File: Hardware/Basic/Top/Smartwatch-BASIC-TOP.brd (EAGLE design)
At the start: 38 x 38 mm, 60 parts, among them SW6 SWITCH.MOM, SW7 SWITCH.MOM, U2 NRF52832_MODULE_MDBT42, U4 FT231XS

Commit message: Top Board Routed
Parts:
- removed C20, C21: 4.7u, LinnesLab-Passives:C0603
- removed C5, C6: 1u, LinnesLab-Passives:C0603
- removed CHRG2: MCP73831, LinnesLab-Power:SOT23-5
- removed LDO2: MIC5504, LinnesLab-Power:SOT23-5
- removed R11: (no value), LinnesLab-Passives:R0603
- removed R12, R15: 100k, LinnesLab-Passives:R0603
- removed SD2: (no value), LinnesLab-Connectors:MICROSD
- moved C14 23.5 mm to (32.9, 13.3)
- moved D1 19.8 mm to (34.6, 12.7), turned to 270 degrees
- moved SW3 19.1 mm to (34.9, 34.8), turned to 90 degrees
- moved R5 16.1 mm to (36.3, 12.9), turned to 270 degrees
- moved LED3 15.3 mm to (34.2, 20.9), turned to 270 degrees
- moved LED4 15.0 mm to (35.8, 20.9), turned to 270 degrees
- moved C17 12.4 mm to (3.27, 19.0)
- moved C19 12.4 mm to (1.95, 19.1)
- moved SW4 12.3 mm to (35.0, 17.0), turned to 270 degrees
- moved CORTEX1 12.0 mm to (35.3, 28.9), turned to 270 degrees
- moved R3 11.3 mm to (33.6, 24.0), turned to 90 degrees
- moved R4 9.96 mm to (36.3, 24.0), turned to 90 degrees
- moved SW7 9.21 mm to (21.9, 4.24), turned to 180 degrees
- moved C11 9.17 mm to (35.4, 9.68), turned to 180 degrees
- moved SW6 8.45 mm to (31.9, 4.24), turned to 180 degrees
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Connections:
- removed net CD2: SD2.CD2
- removed net N$17: CHRG2.5, R11.2
- net 3.3V: no longer C6.1, LDO2.5, R15.2, SD2.4
- net D27/CHRG.STAT: no longer CHRG2.1, R12.1
- net D5/CD1: no longer SD2.CD1
- net D7/SD.CS: no longer SD2.2
- net GND: no longer C20.2, C21.1, C5.1, C6.2, CHRG2.2, LDO2.2, R11.1, R15.1, SD2.6, SD2.MT1, SD2.MT2
- net MISO: no longer SD2.7
- net MOSI: no longer SD2.3
- net SCK: no longer SD2.5
- net VIN: no longer C21.2, C5.2, CHRG2.4, LDO2.1, LDO2.3, R12.2
- net VLIPO: no longer C20.1, CHRG2.3
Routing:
- net SCK: track 59.4 -> 17.7 mm, vias 2 -> 0
- net D27/CHRG.STAT: track 33.4 -> 0.00 mm, vias 1 -> 0
- net D7/SD.CS: track 31.7 -> 3.52 mm
- net MOSI: track 42.1 -> 15.0 mm, vias 5 -> 2
- net RESET: track 0.00 -> 26.1 mm, vias 0 -> 2
- net GND: track 90.5 -> 113.5 mm, vias 22 -> 23
- net D3/RESET.OLED: track 34.8 -> 12.8 mm
- net 3.3V: track 58.4 -> 38.2 mm, vias 13 -> 11
- net MISO: track 19.6 -> 0.00 mm, vias 3 -> 0
- net P0.09/NFC1: track 3.11 -> 19.9 mm, vias 0 -> 2
- net VIN: track 31.4 -> 15.3 mm
- net D5/CD1: track 14.4 -> 0.00 mm, vias 1 -> 0
- net LED2: track 0.00 -> 13.0 mm, vias 0 -> 2
- net RXD: track 29.0 -> 40.4 mm
- net N$2: track 3.22 -> 14.0 mm, vias 0 -> 2
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
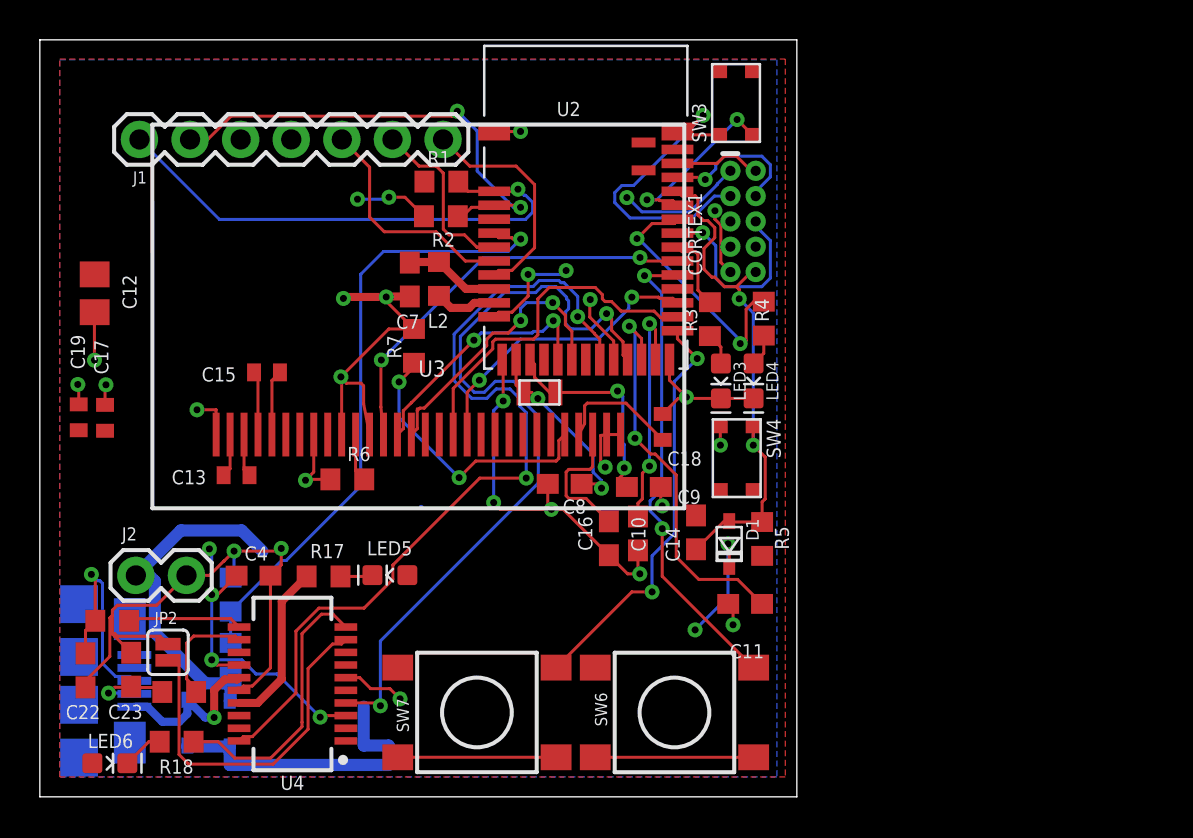
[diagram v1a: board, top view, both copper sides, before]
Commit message: Rearranging Top Board
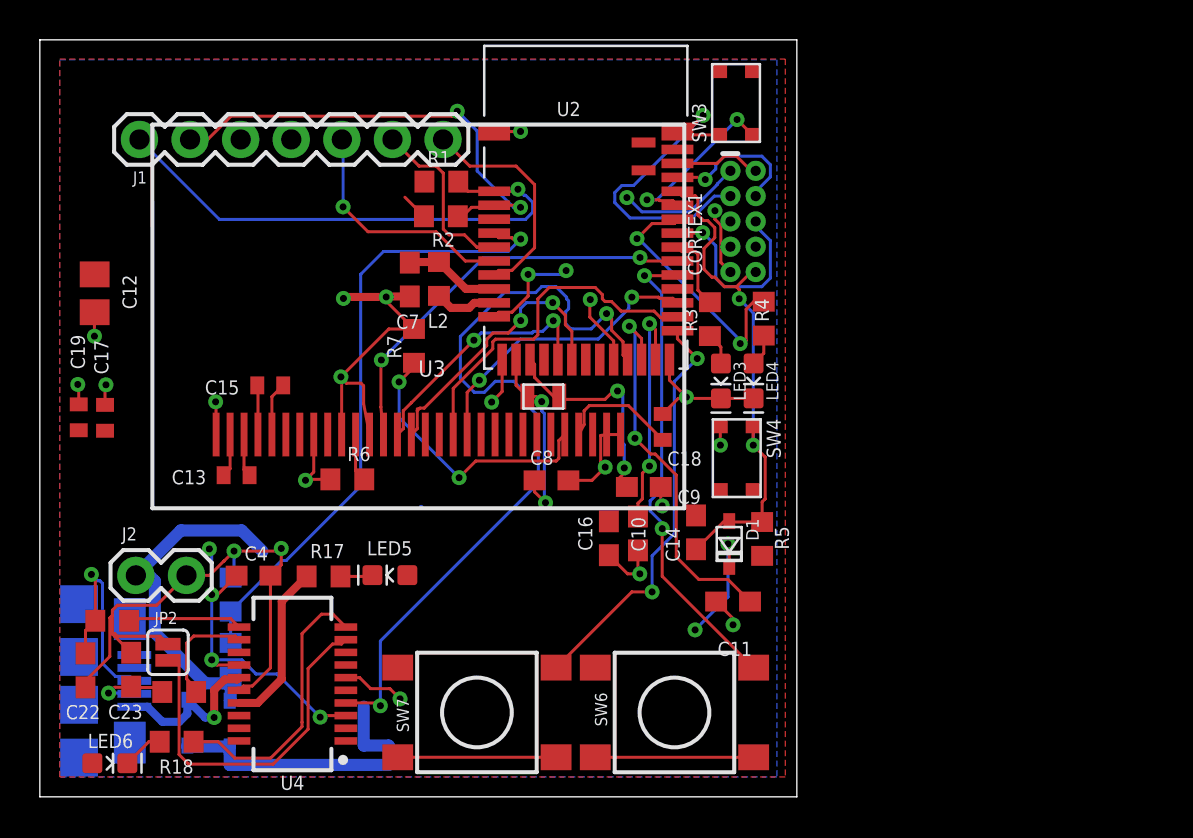
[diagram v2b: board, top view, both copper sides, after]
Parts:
- moved C8 0.69 mm to (25.7, 15.9), turned to 180 degrees
- moved C15 0.67 mm to (11.6, 20.7)
- moved C11 0.62 mm to (34.8, 9.80)
- moved XTAL2 0.28 mm to (25.3, 20.1)
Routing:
- net TXD: track 43.9 -> 0.00 mm, vias 2 -> 0
- net GND: track 113.5 -> 101.0 mm, vias 23 -> 21
- net N$13: track 7.57 -> 0.00 mm
- net 3.3V: track 38.2 -> 35.8 mm, vias 11 -> 9
- net N$7: track 3.20 -> 2.48 mm
- net P0.09/NFC1: track 19.9 -> 19.2 mm
- net N$8: track 3.29 -> 2.70 mm
- net A6/TIA: track 11.6 -> 12.1 mm, vias 0 -> 1

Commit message: Rearranged Top Board
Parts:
- moved C9 3.18 mm to (28.1, 13.3), turned to 270 degrees
- moved C16 3.01 mm to (30.3, 15.4), turned to 180 degrees
- moved C18 0.91 mm to (31.2, 19.5)
- moved C11 0.43 mm to (35.2, 9.89), turned to 0 degrees
- moved R7 0.19 mm to (18.9, 22.8)
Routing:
- net TXD: track 0.00 -> 32.8 mm, vias 0 -> 2
- net 3.3V: track 35.8 -> 29.6 mm, vias 9 -> 7
- net LED2: track 13.0 -> 9.38 mm
- net N$13: track 0.00 -> 3.44 mm
- net GND: track 101.0 -> 98.6 mm
- net VIN: track 15.3 -> 13.3 mm
- net N$6: track 11.1 -> 10.0 mm
- net USB-: track 4.77 -> 4.04 mm
- net SDA: track 26.3 -> 26.9 mm

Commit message: Rearranged Top Board
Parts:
- added C1, C3: 4.7u, LinnesLab-Passives:C0603
- added C5, C6: 1u, LinnesLab-Passives:C0603
- added CHRG2: MCP73831, LinnesLab-Power:SOT23-5
- added LDO2: MIC5504, LinnesLab-Power:SOT23-5
- added R11: (no value), LinnesLab-Passives:R0603
- added R12, R8: 100k, LinnesLab-Passives:R0603
- moved C12 6.90 mm to (2.32, 32.2)
- moved C17 5.82 mm to (3.08, 13.2)
- moved C19 5.82 mm to (1.76, 13.2)
- moved C18 0.71 mm to (31.6, 20.1), turned to 180 degrees
- moved XTAL2 0.20 mm to (25.1, 20.2)
- moved R2 0.14 mm to (20.1, 29.0)
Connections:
- new net N$16: CHRG2.5, R11.2
- new net VIN1: C1.2, C5.2, CHRG2.4, LDO2.1, LDO2.3, R12.2
- net 3.3V: now also C6.1, LDO2.5, R8.2
- net D27/CHRG.STAT: now also CHRG2.1, R12.1
- net GND: now also C1.1, C3.2, C5.1, C6.2, CHRG2.2, LDO2.2, R11.1, R8.1
- net VLIPO: now also C3.1, CHRG2.3
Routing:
- net D27/CHRG.STAT: track 0.00 -> 26.5 mm, vias 0 -> 2
- net 3.3V: track 29.6 -> 9.59 mm, vias 7 -> 1
- net RXD: track 40.4 -> 24.9 mm
- net VIN1: track 0.00 -> 13.5 mm
- net VLIPO: track 17.6 -> 11.3 mm
- net USB+: track 11.0 -> 4.91 mm
- net SCL: track 23.6 -> 17.5 mm, vias 2 -> 0
- net SDA: track 26.9 -> 21.5 mm, vias 1 -> 0
- net A4/BATT: track 31.6 -> 26.5 mm
- net GND: track 98.6 -> 94.3 mm, vias 21 -> 29
- net P0.09/NFC1: track 19.5 -> 15.2 mm
- net A6/TIA: track 12.1 -> 15.9 mm, vias 1 -> 0
- net P0.10/NFC2: track 11.8 -> 8.74 mm, vias 2 -> 0
- net TXD: track 32.8 -> 35.3 mm
- net A7/PPG: track 11.6 -> 9.55 mm, vias 0 -> 1
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
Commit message: Fixing top board issues
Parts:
- moved C19 6.21 mm to (7.96, 12.9), turned to 90 degrees
- moved J2 5.11 mm to (2.34, 12.1), turned to 90 degrees
- moved C17 3.58 mm to (6.64, 12.9), turned to 90 degrees
- moved LED4 0.30 mm to (35.5, 20.9)
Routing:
- net VIN: track 12.1 -> 2.17 mm
- net VLIPO: track 11.3 -> 18.0 mm
- net 3.3V: track 9.59 -> 6.37 mm
- net GND: track 94.3 -> 96.6 mm, vias 29 -> 30
- net D4/DC.OLED: track 14.2 -> 15.2 mm
- net N$4: track 9.45 -> 8.87 mm
- net A6/TIA: track 15.9 -> 16.5 mm
- net D3/RESET.OLED: track 12.8 -> 13.3 mm
- net D11/SW1: track 22.0 -> 22.5 mm

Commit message: Top Board Complete
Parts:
- moved C19 11.8 mm to (2.93, 2.28)
- moved C17 11.8 mm to (1.61, 2.30)
- moved C23 5.45 mm to (6.56, 11.5), turned to 180 degrees
- moved R10 3.81 mm to (8.19, 8.88), turned to 270 degrees
- moved LED6 2.80 mm to (4.55, 4.29), turned to 270 degrees
- moved C22 2.10 mm to (3.91, 7.69), turned to 0 degrees
- moved C1 1.48 mm to (6.17, 17.5)
- moved R18 0.98 mm to (6.97, 3.74)
- moved C11 0.59 mm to (35.4, 9.33)
- moved R16 0.43 mm to (3.98, 9.09)
- moved C9 0.42 mm to (27.6, 13.4)
- moved XTAL2 0.07 mm to (25.0, 20.2)
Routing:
- net USB-: track 4.37 -> 13.6 mm
- net GND: track 96.6 -> 88.5 mm, vias 30 -> 29
- net USB+: track 4.91 -> 8.57 mm
- net N$25: track 4.23 -> 1.87 mm
- net V_USB: track 8.63 -> 7.15 mm
- net !CTS: track 18.5 -> 17.6 mm
- net N$4: track 8.87 -> 8.02 mm
- net RESET: track 26.1 -> 25.3 mm
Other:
- board text added: "+"

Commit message: Organized Schematics and Silkscreens for both boards
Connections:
- removed net VIN1: C1.2, C5.2, CHRG2.4, LDO2.1, LDO2.3, R12.2
- net VIN: now also C1.2, C5.2, CHRG2.4, LDO2.1, LDO2.3, R12.2
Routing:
- net VIN: track 2.17 -> 15.6 mm
- net VIN1: track 13.4 -> 0.00 mm
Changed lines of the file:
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@@
 <wire x1="3.175" y1="25.679396875" x2="3.210559375" y2="25.71495625" width="0.1524" layer="1"/>
 <via x="3.210559375" y="25.71495625" extent="1-16" drill="0.35"/>
-<wire x1="32.231678125" y1="20.0924" x2="32.355875" y2="20.216596875" width="0.1524" layer="1"/>
 <wire x1="3.6846375" y1="16.863059375" x2="3.971659375" y2="16.5760375" width="0.1524" layer="1"/>
 <wire x1="3.971659375" y1="16.5760375" x2="4.91744375" y2="16.576040625" width="0.1524" layer="1"/>
@@
 <wire x1="7.404865625" y1="2.57514375" x2="7.404865625" y2="2.52688125" width="0.6096" layer="16"/>
 <wire x1="7.404865625" y1="2.52688125" x2="9.530840625" y2="2.52688125" width="0.6096" layer="16"/>
+<contactref element="C5" pad="2"/>
+<contactref element="LDO2" pad="1"/>
+<contactref element="LDO2" pad="3"/>
+<contactref element="CHRG2" pad="4"/>
+<contactref element="C1" pad="2"/>
+<contactref element="R12" pad="2"/>
+<wire x1="4.563996875" y1="18.5953" x2="5.90718125" y2="18.5953" width="0.6096" layer="1"/>
+<wire x1="6.1696625" y1="18.33281875" x2="5.90718125" y2="18.5953" width="0.6096" layer="1"/>
+<wire x1="4.563996875" y1="18.5953" x2="3.48651875" y2="19.672778125" width="0.6096" layer="1"/>
+<wire x1="3.48651875" y1="19.672778125" x2="3.48651875" y2="22.0370375" width="0.6096" layer="1"/>
+<wire x1="4.125" y1="24.56979375" x2="4.125" y2="22.67551875" width="0.6096" layer="1"/>
+<wire x1="4.125" y1="22.67551875" x2="3.48651875" y2="22.0370375" width="0.6096" layer="1"/>
+<wire x1="5.95375625" y1="24.2350375" x2="5.619" y2="24.56979375" width="0.6096" layer="1"/>
+<wire x1="5.619" y1="24.56979375" x2="4.125" y2="24.56979375" width="0.6096" layer="1"/>
+<wire x1="2.225" y1="24.56979375" x2="2.4428" y2="24.35199375" width="0.6096" layer="1"/>
+<wire x1="2.4428" y1="24.35199375" x2="2.4428" y2="23.7804125" width="0.6096" layer="1"/>
+<wire x1="3.48651875" y1="22.73669375" x2="3.48651875" y2="22.0370375" width="0.6096" layer="1"/>
+<wire x1="2.4428" y1="23.7804125" x2="3.48651875" y2="22.73669375" width="0.6096" layer="1"/>
+<wire x1="7.404865625" y1="2.57514375" x2="6.1696625" y2="18.33281875" width="0" layer="19" extent="1-16"/>
 </signal>
 <signal name="N$21">
@@
 <wire x1="4.563996875" y1="21.36011875" x2="5.17741875" y2="21.973540625" width="0.1524" layer="1"/>
 </signal>
-<signal name="VIN1">
-<contactref element="C5" pad="2"/>
-<contactref element="LDO2" pad="1"/>
-<contactref element="LDO2" pad="3"/>
-<contactref element="CHRG2" pad="4"/>
-<contactref element="C1" pad="2"/>
-<contactref element="R12" pad="2"/>
-<wire x1="4.563996875" y1="18.5953" x2="5.90718125" y2="18.5953" width="0.6096" layer="1"/>
-<wire x1="6.1696625" y1="18.33281875" x2="5.90718125" y2="18.5953" width="0.6096" layer="1"/>
-<wire x1="4.563996875" y1="18.5953" x2="3.48651875" y2="19.672778125" width="0.6096" layer="1"/>
-<wire x1="3.48651875" y1="19.672778125" x2="3.48651875" y2="22.0370375" width="0.6096" layer="1"/>
-<wire x1="4.125" y1="24.56979375" x2="4.125" y2="22.67551875" width="0.6096" layer="1"/>
-<wire x1="4.125" y1="22.67551875" x2="3.48651875" y2="22.0370375" width="0.6096" layer="1"/>
-<wire x1="5.95375625" y1="24.2350375" x2="5.619" y2="24.56979375" width="0.6096" layer="1"/>
-<wire x1="5.619" y1="24.56979375" x2="4.125" y2="24.56979375" width="0.6096" layer="1"/>
-<wire x1="2.225" y1="24.56979375" x2="2.4428" y2="24.35199375" width="0.6096" layer="1"/>
-<wire x1="2.4428" y1="24.35199375" x2="2.4428" y2="23.7804125" width="0.6096" layer="1"/>
-<wire x1="3.48651875" y1="22.73669375" x2="3.48651875" y2="22.0370375" width="0.6096" layer="1"/>
-<wire x1="2.4428" y1="23.7804125" x2="3.48651875" y2="22.73669375" width="0.6096" layer="1"/>
-</signal>
 </signals>

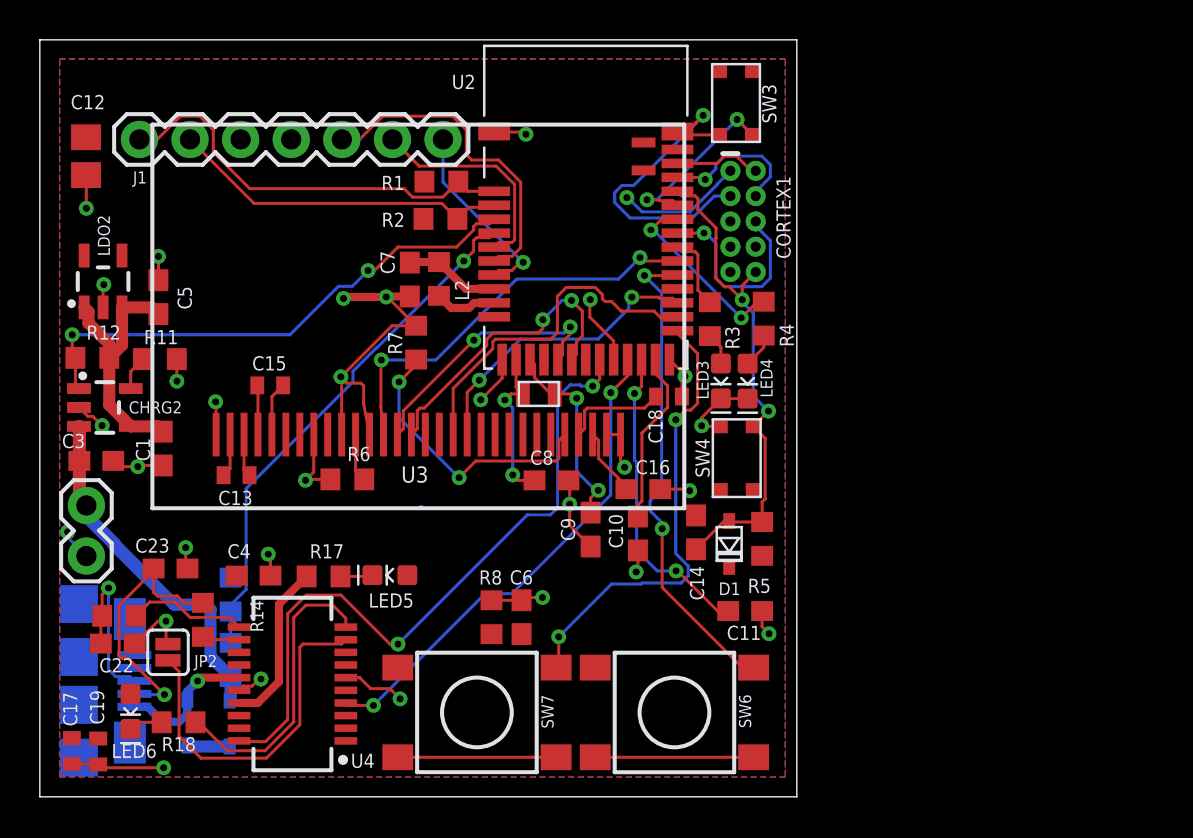
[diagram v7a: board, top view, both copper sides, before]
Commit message: Fixed Top Board Issue
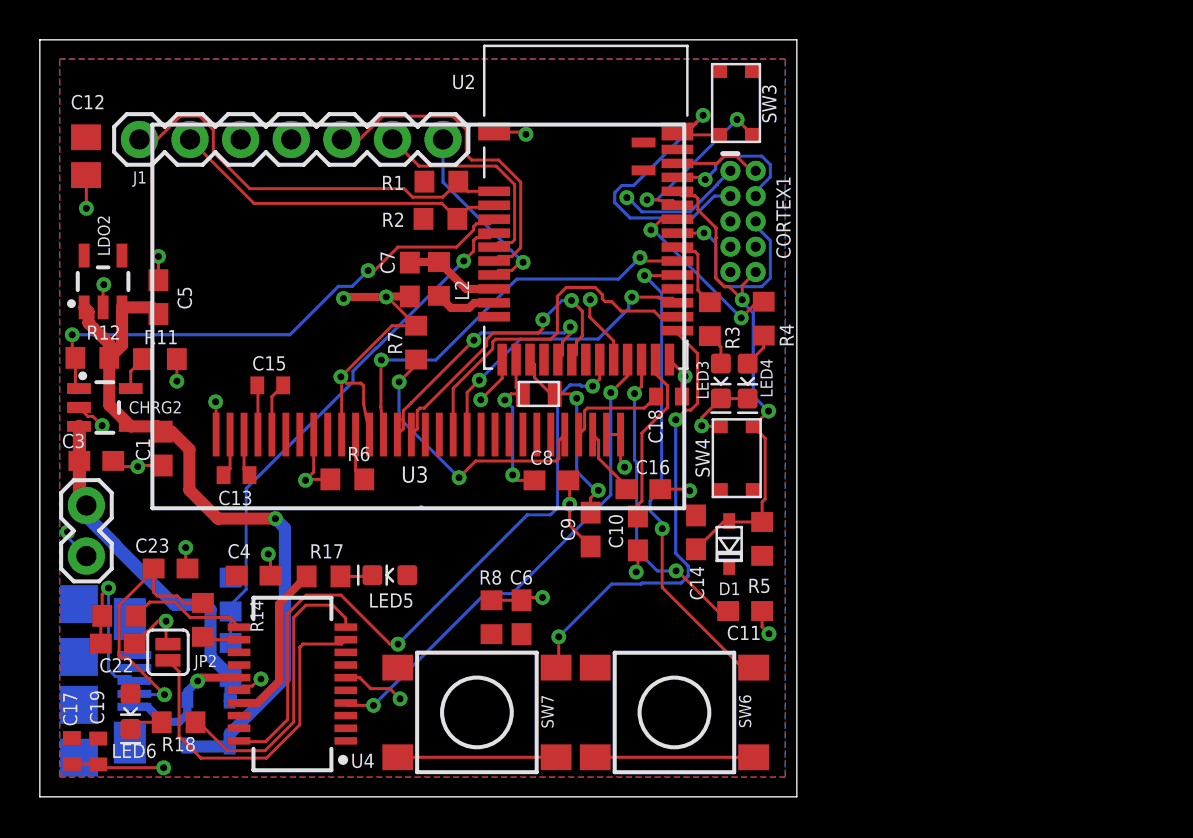
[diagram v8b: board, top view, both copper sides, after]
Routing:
- net VIN: track 15.6 -> 37.0 mm, vias 0 -> 1
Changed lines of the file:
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@@
 <drawing>
 <settings>
-<setting alwaysvectorfont="no"/>
+<setting alwaysvectorfont="yes"/>
 <setting verticaltext="up"/>
 </settings>
@@
 <via x="18.082259375" y="4.91998125" extent="1-16" drill="0.35"/>
 <contactref element="J1" pad="3"/>
-<wire x1="32.006" y1="33.397" x2="32.0942" y2="33.4852" width="0.1524" layer="1"/>
 <wire x1="18.570740625" y1="25.1173625" x2="17.4117625" y2="25.1173625" width="0.4064" layer="1"/>
 <wire x1="17.4117625" y1="25.1173625" x2="17.387059375" y2="25.092659375" width="0.4064" layer="1"/>
@@
 <wire x1="3.48651875" y1="22.73669375" x2="3.48651875" y2="22.0370375" width="0.6096" layer="1"/>
 <wire x1="2.4428" y1="23.7804125" x2="3.48651875" y2="22.73669375" width="0.6096" layer="1"/>
-<wire x1="7.404865625" y1="2.57514375" x2="6.1696625" y2="18.33281875" width="0" layer="19" extent="1-16"/>
+<wire x1="9.530840625" y1="2.52688125" x2="9.530840625" y2="3.161609375" width="0.6096" layer="16"/>
+<wire x1="9.530840625" y1="3.161609375" x2="12.3009625" y2="5.93173125" width="0.6096" layer="16"/>
+<wire x1="6.1696625" y1="18.33281875" x2="6.6176" y2="18.33281875" width="0.6096" layer="1"/>
+<wire x1="7.508240625" y1="15.39748125" x2="7.508240625" y2="17.442178125" width="0.6096" layer="1"/>
+<wire x1="6.6176" y1="18.33281875" x2="7.508240625" y2="17.442178125" width="0.6096" layer="1"/>
+<wire x1="12.3009625" y1="13.48765625" x2="11.8237" y2="13.96491875" width="0.6096" layer="16"/>
+<via x="11.8237" y="13.96491875" extent="1-16" drill="0.35"/>
+<wire x1="11.8237" y1="13.96491875" x2="8.940803125" y2="13.96491875" width="0.6096" layer="1"/>
+<wire x1="12.3009625" y1="5.93173125" x2="12.3009625" y2="13.48765625" width="0.6096" layer="16"/>
+<wire x1="8.940803125" y1="13.96491875" x2="7.508240625" y2="15.39748125" width="0.6096" layer="1"/>
 </signal>
 <signal name="N$21">
